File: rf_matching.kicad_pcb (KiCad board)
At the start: 2 copper layers, 46.6 x 32.6 mm, 12 parts, among them J1 RFI, J2 RFO, J3 CTRL, J4 ANT, J5 3V3, U1 pe4259ds, U2 SF2098

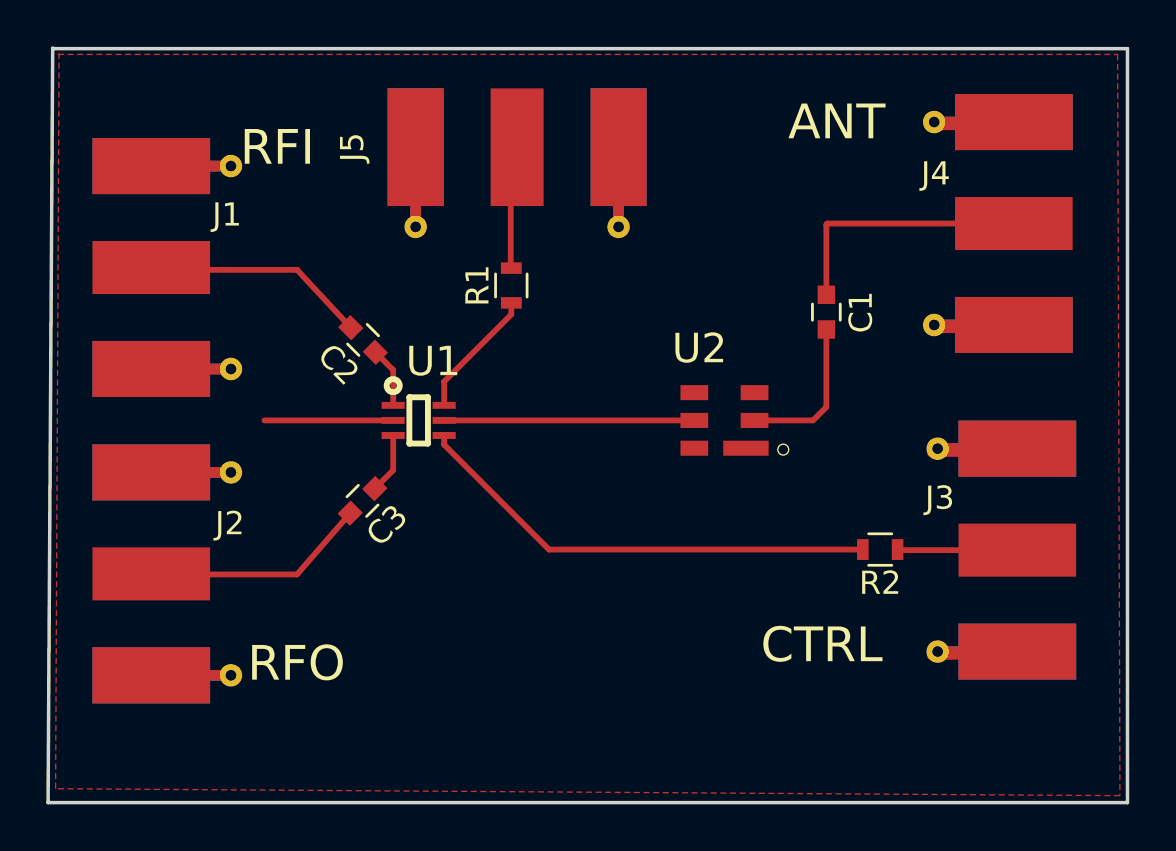
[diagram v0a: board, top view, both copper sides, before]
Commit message: Version with the board with just the saw filter, no vias yet
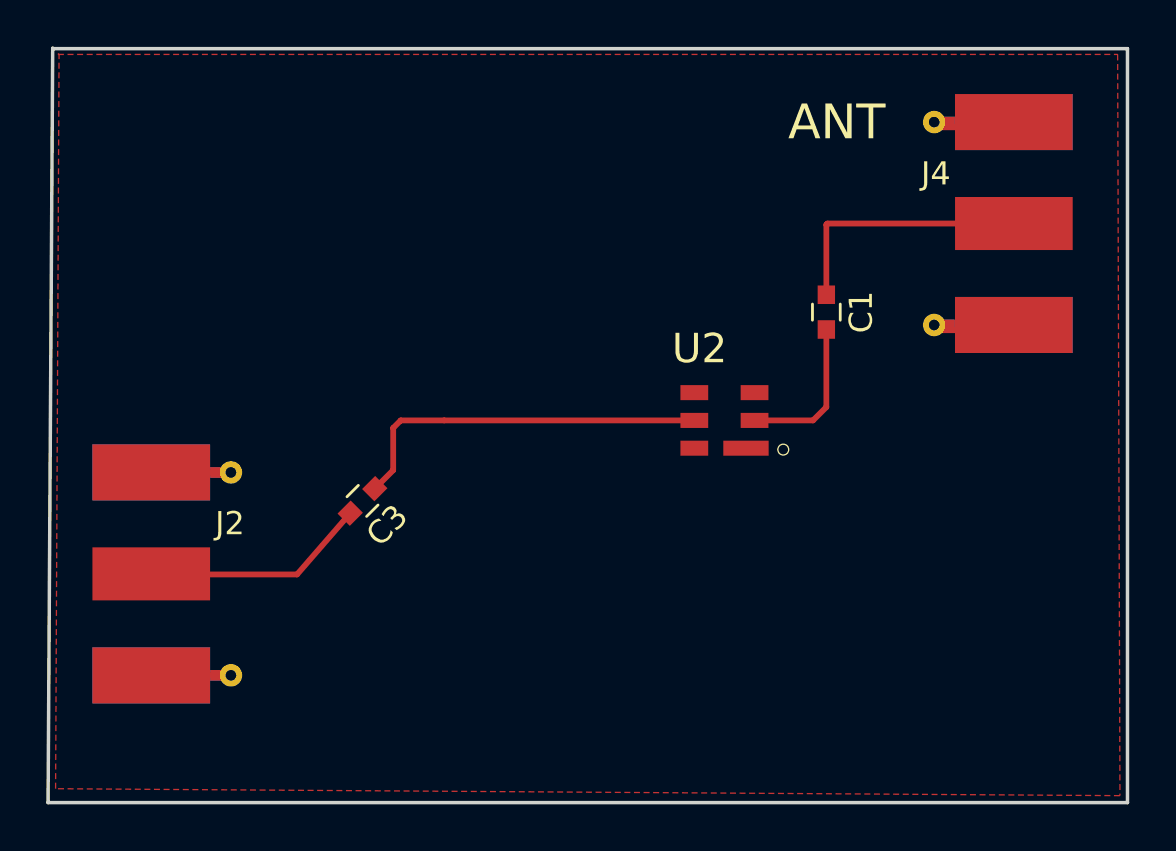
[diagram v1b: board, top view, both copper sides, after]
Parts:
- removed C2: 1uF, KiCad/Capacitors_SMD.pretty:C_0603
- removed J1: RFI, KiCad/Connectors_Molex.pretty:Molex_SMA_Jack_Edge_Mount
- removed J3: CTRL, KiCad/Connectors_Molex.pretty:Molex_SMA_Jack_Edge_Mount
- removed J5: 3V3, KiCad/Connectors_Molex.pretty:Molex_SMA_Jack_Edge_Mount
- removed R1, R2: 1K, KiCad/Resistors_SMD.pretty:R_0603
- removed U1: pe4259ds, OLIMEX/KiCAD/KiCAD_Footprints/OLIMEX_IC-FP.pretty:SC70-6_Pitch-0.65_2.00x2.10x1.00mm
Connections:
- U2 pad 5: Net-(U1-Pad5) -> Net-(C3-Pad1)
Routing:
- net GND: track 46.8 -> 13.8 mm
- net Net-(R2-Pad2): track 20.3 -> 0.00 mm
- net Net-(C3-Pad1): track 2.62 -> 16.1 mm
- net Net-(U1-Pad5): track 10.8 -> 0.00 mm
- net Net-(C2-Pad2): track 10.4 -> 0.00 mm
- net Net-(R1-Pad1): track 5.63 -> 0.00 mm
- net Net-(J5-Pad1): track 5.26 -> 0.00 mm
- net Net-(J3-Pad1): track 5.18 -> 0.00 mm
- net Net-(C2-Pad1): track 2.61 -> 0.00 mm
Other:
- board text removed: "CTRL"
- board text removed: "RFI"
- board text removed: "RFO"
